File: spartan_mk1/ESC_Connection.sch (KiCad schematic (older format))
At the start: 2 parts

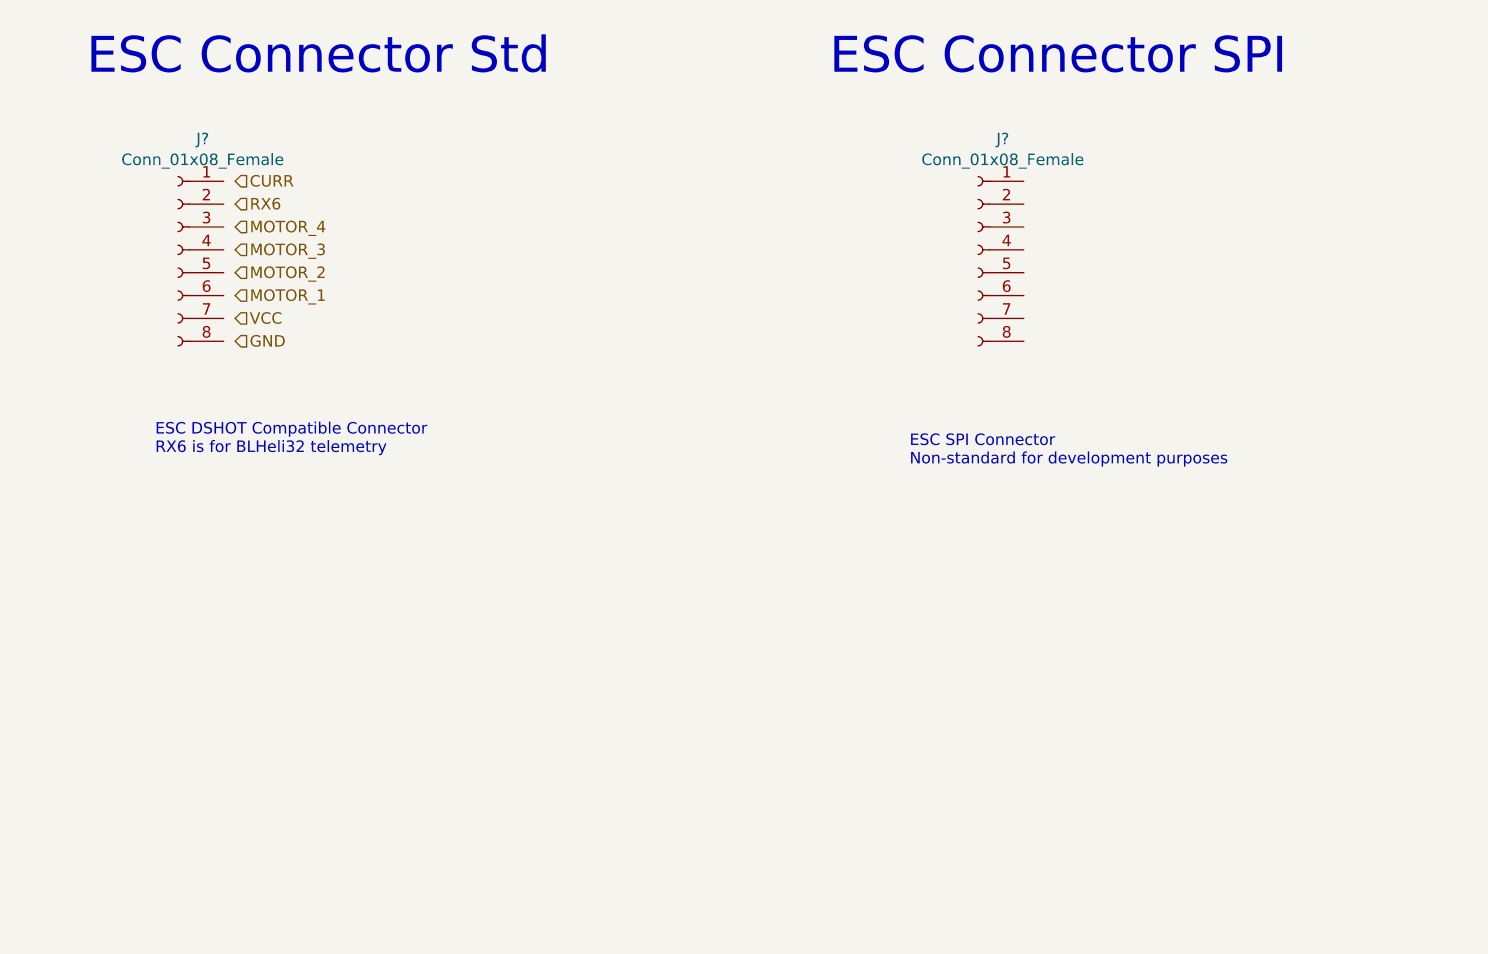
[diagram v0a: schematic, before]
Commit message: Added ESC connectors in schematic
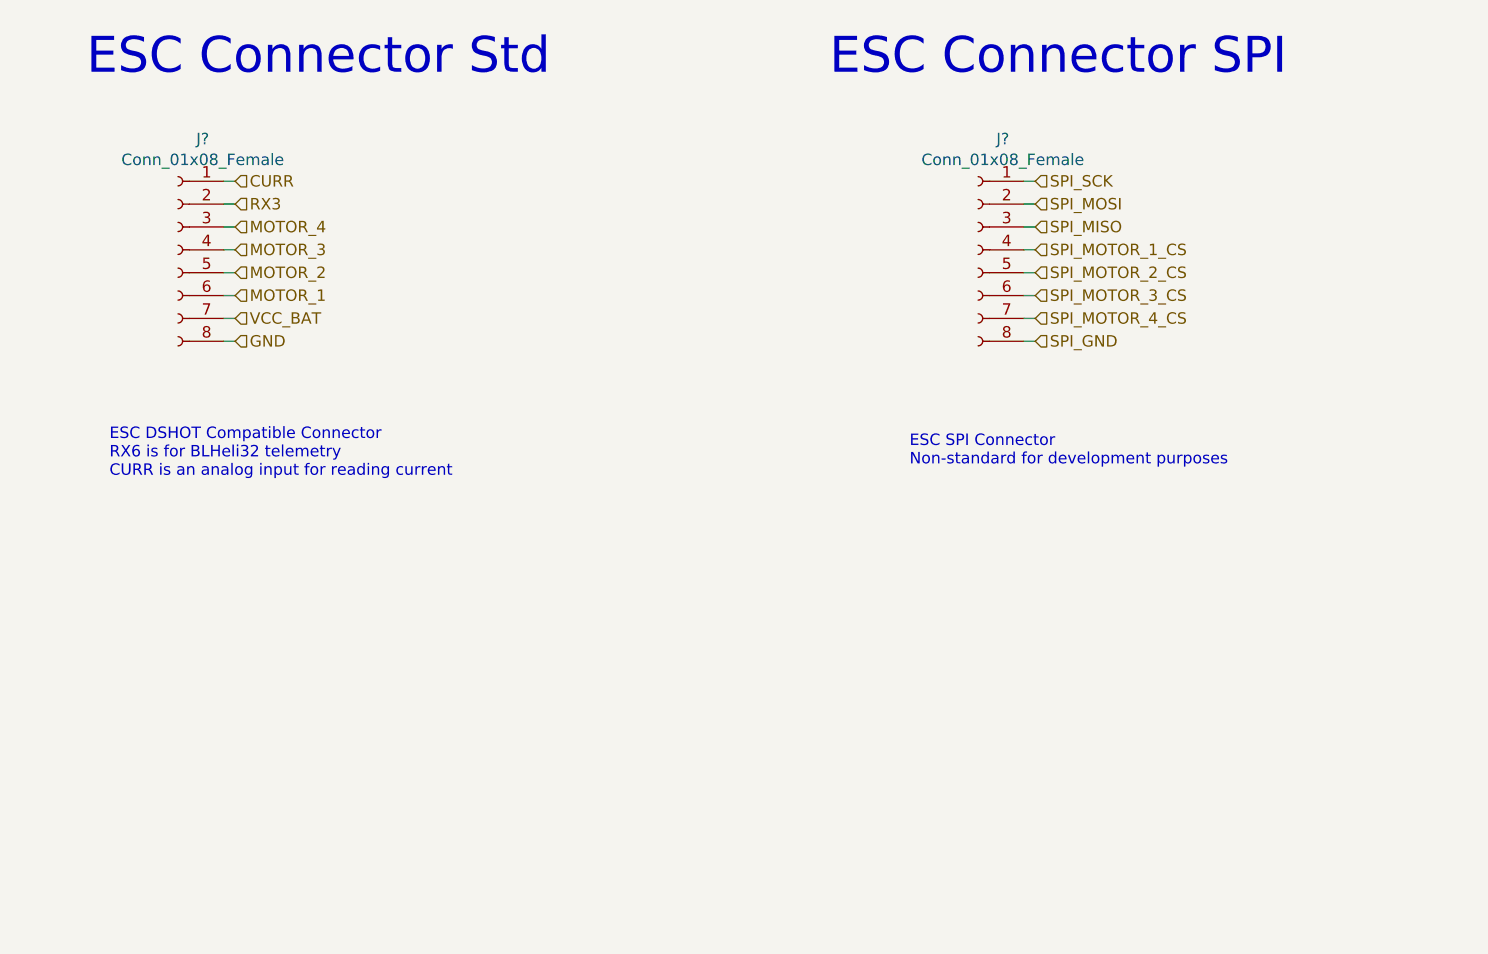
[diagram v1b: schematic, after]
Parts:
- removed J?: Conn_01x08_Female, symbol Connector:Conn_01x08_Female
- added J?: Conn_01x08_Female, symbol Connector:Conn_01x08_Female
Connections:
- net CURR: now also J?.1 (Pin_1)
- net GND: now also J?.8 (Pin_8)
- net MOTOR_1: now also J?.6 (Pin_6)
- net MOTOR_2: now also J?.5 (Pin_5)
- net MOTOR_3: now also J?.4 (Pin_4)
- net MOTOR_4: now also J?.3 (Pin_3)
- net RX3: now reaches J?.2 (Pin_2)
- net VCC_BAT: now reaches J?.7 (Pin_7)
- new net SPI_GND: J?.8 (Pin_8)
- new net SPI_MISO: J?.3 (Pin_3)
- new net SPI_MOSI: J?.2 (Pin_2)
- new net SPI_MOTOR_1_CS: J?.4 (Pin_4)
- new net SPI_MOTOR_2_CS: J?.5 (Pin_5)
- new net SPI_MOTOR_3_CS: J?.6 (Pin_6)
- new net SPI_MOTOR_4_CS: J?.7 (Pin_7)
- new net SPI_SCK: J?.1 (Pin_1)
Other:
- note added: "ESC DSHOT Compatible Connector\nRX6 is for BLHeli32 telemetry\nCURR is an analog input for reading current"
- note removed: "ESC DSHOT Compatible Connector\nRX6 is for BLHeli32 telemetry\n"
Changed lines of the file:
@@
 	-1   0    0    -1
 $EndComp
-Text Notes 3550 4000 0    50   ~ 0
-ESC DSHOT Compatible Connector\nRX6 is for BLHeli32 telemetry\n
+Text Notes 3350 4100 0    50   ~ 0
+ESC DSHOT Compatible Connector\nRX6 is for BLHeli32 telemetry\nCURR is an analog input for reading current
 Text Notes 3250 2350 0    157  ~ 0
 ESC Connector Std
 Text Notes 6500 2350 0    157  ~ 0
 ESC Connector SPI
-$Comp
-L Connector:Conn_01x08_Female J?
-U 1 1 5FC07A5E
-P 7150 3100
-F 0 "J?" H 7042 3585 50  0000 C CNN
-F 1 "Conn_01x08_Female" H 7042 3494 50  0000 C CNN
-F 2 "" H 7150 3100 50  0001 C CNN
-F 3 "~" H 7150 3100 50  0001 C CNN
-	1    7150 3100
-	-1   0    0    -1
-$EndComp
 Text Notes 6850 4050 0    50   ~ 0
 ESC SPI Connector\nNon-standard for development purposes\n
@@
 GND
 Text HLabel 3900 3400 2    50   Input ~ 0
-VCC
+VCC_BAT
 Text HLabel 3900 3300 2    50   Input ~ 0
 MOTOR_1
@@
 MOTOR_4
 Text HLabel 3900 2900 2    50   Input ~ 0
-RX6
+RX3
 Text HLabel 3900 2800 2    50   Input ~ 0
 CURR
+Wire Wire Line
+	3900 3500 3850 3500
+Wire Wire Line
+	3900 3400 3850 3400
+Wire Wire Line
+	3900 3300 3850 3300
+Wire Wire Line
+	3900 3200 3850 3200
+Wire Wire Line
+	3900 3100 3850 3100
+Wire Wire Line
+	3900 3000 3850 3000
+Wire Wire Line
+	3900 2900 3850 2900
+Wire Wire Line
+	3900 2800 3850 2800
+Wire Wire Line
+	7400 2800 7350 2800
+Text HLabel 7400 2800 2    50   Input ~ 0
+SPI_SCK
+Text HLabel 7400 2900 2    50   Input ~ 0
+SPI_MOSI
+Text HLabel 7400 3000 2    50   Input ~ 0
+SPI_MISO
+Wire Wire Line
+	7400 2900 7350 2900
+Wire Wire Line
+	7400 3000 7350 3000
+Text HLabel 7400 3100 2    50   Input ~ 0
+SPI_MOTOR_1_CS
+Text HLabel 7400 3200 2    50   Input ~ 0
+SPI_MOTOR_2_CS
+Text HLabel 7400 3300 2    50   Input ~ 0
+SPI_MOTOR_3_CS
+Text HLabel 7400 3400 2    50   Input ~ 0
+SPI_MOTOR_4_CS
+Wire Wire Line
+	7400 3100 7350 3100
+Wire Wire Line
+	7400 3200 7350 3200
+Wire Wire Line
+	7400 3300 7350 3300
+Wire Wire Line
+	7400 3400 7350 3400
+Text HLabel 7400 3500 2    50   Input ~ 0
+SPI_GND
+Wire Wire Line
+	7400 3500 7350 3500
+$Comp
+L Connector:Conn_01x08_Female J?
+U 1 1 5F8D6084
+P 7150 3100
+F 0 "J?" H 7042 3585 50  0000 C CNN
+F 1 "Conn_01x08_Female" H 7042 3494 50  0000 C CNN
+F 2 "" H 7150 3100 50  0001 C CNN
+F 3 "~" H 7150 3100 50  0001 C CNN
+	1    7150 3100
+	-1   0    0    -1
+$EndComp
 $EndSCHEMATC

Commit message: Complete schematic with DRC done
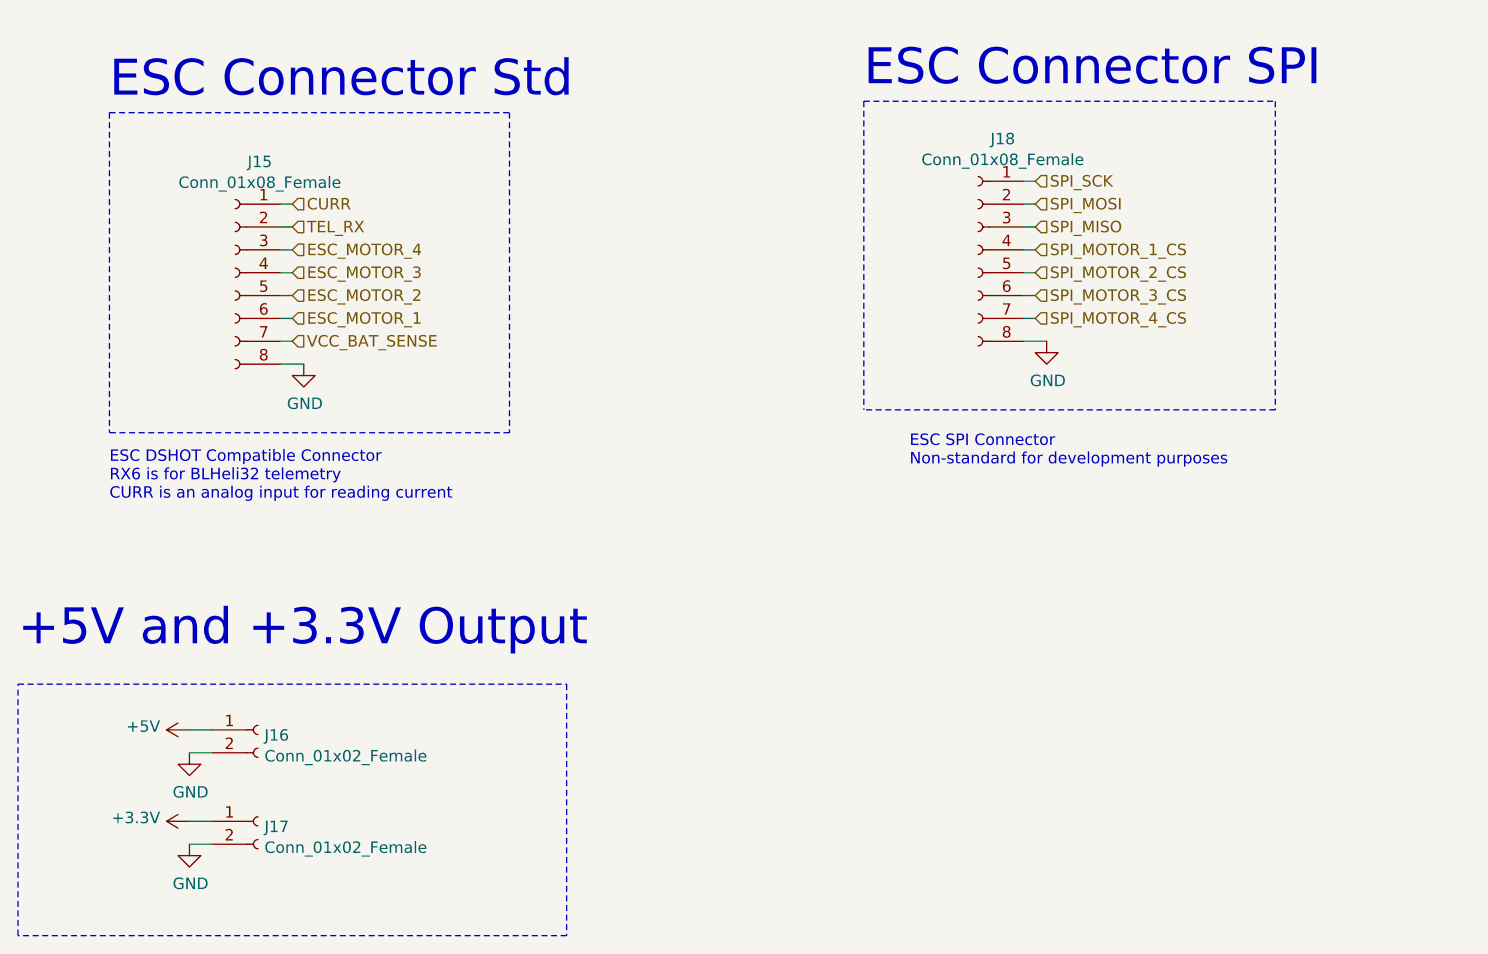
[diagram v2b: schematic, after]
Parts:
- added J16, J17: Conn_01x02_Female, symbol Connector:Conn_01x02_Female
- gave numbers to parts that had none: 2
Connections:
- net SPI_GND is gone; now on net GND: J18.8 (Pin_8)
- net GND: now also J16.2 (Pin_2), J17.2 (Pin_2)
- net MOTOR_1 renamed ESC_MOTOR_1
- net MOTOR_2 renamed ESC_MOTOR_2
- net MOTOR_3 renamed ESC_MOTOR_3
- net MOTOR_4 renamed ESC_MOTOR_4
- net RX3 renamed TEL_RX
- net VCC_BAT renamed VCC_BAT_SENSE
- new net +3V3: J17.1 (Pin_1)
- new net +5V: J16.1 (Pin_1)
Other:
- note added: "+5V and +3.3V Output"
- moved on the sheet: J15
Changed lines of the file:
@@
 $Descr A4 11693 8268
 encoding utf-8
-Sheet 5 6
+Sheet 6 6
 Title ""
 Date ""
@@
 $EndDescr
 $Comp
-L Connector:Conn_01x08_Female J?
+L Connector:Conn_01x08_Female J15
 U 1 1 5FC05E26
-P 3650 3100
-F 0 "J?" H 3542 3585 50  0000 C CNN
-F 1 "Conn_01x08_Female" H 3542 3494 50  0000 C CNN
-F 2 "" H 3650 3100 50  0001 C CNN
-F 3 "~" H 3650 3100 50  0001 C CNN
-	1    3650 3100
+P 3900 3200
+F 0 "J15" H 3792 3685 50  0000 C CNN
+F 1 "Conn_01x08_Female" H 3792 3594 50  0000 C CNN
+F 2 "" H 3900 3200 50  0001 C CNN
+F 3 "~" H 3900 3200 50  0001 C CNN
+	1    3900 3200
 	-1   0    0    -1
 $EndComp
-Text Notes 3350 4100 0    50   ~ 0
+Text Notes 3350 4200 0    50   ~ 0
 ESC DSHOT Compatible Connector\nRX6 is for BLHeli32 telemetry\nCURR is an analog input for reading current
-Text Notes 3250 2350 0    157  ~ 0
+Text Notes 3350 2450 0    157  ~ 0
 ESC Connector Std
-Text Notes 6500 2350 0    157  ~ 0
+Text Notes 6650 2400 0    157  ~ 0
 ESC Connector SPI
 Text Notes 6850 4050 0    50   ~ 0
 ESC SPI Connector\nNon-standard for development purposes\n
-Text HLabel 3900 3500 2    50   Input ~ 0
-GND
-Text HLabel 3900 3400 2    50   Input ~ 0
-VCC_BAT
-Text HLabel 3900 3300 2    50   Input ~ 0
-MOTOR_1
-Text HLabel 3900 3200 2    50   Input ~ 0
-MOTOR_2
-Text HLabel 3900 3100 2    50   Input ~ 0
-MOTOR_3
-Text HLabel 3900 3000 2    50   Input ~ 0
-MOTOR_4
-Text HLabel 3900 2900 2    50   Input ~ 0
-RX3
-Text HLabel 3900 2800 2    50   Input ~ 0
+Text HLabel 4150 3500 2    50   Input ~ 0
+VCC_BAT_SENSE
+Text HLabel 4150 3400 2    50   Input ~ 0
+ESC_MOTOR_1
+Text HLabel 4150 3300 2    50   Input ~ 0
+ESC_MOTOR_2
+Text HLabel 4150 3200 2    50   Input ~ 0
+ESC_MOTOR_3
+Text HLabel 4150 3100 2    50   Input ~ 0
+ESC_MOTOR_4
+Text HLabel 4150 3000 2    50   Input ~ 0
+TEL_RX
+Text HLabel 4150 2900 2    50   Input ~ 0
 CURR
 Wire Wire Line
-	3900 3500 3850 3500
-Wire Wire Line
-	3900 3400 3850 3400
-Wire Wire Line
-	3900 3300 3850 3300
-Wire Wire Line
-	3900 3200 3850 3200
-Wire Wire Line
-	3900 3100 3850 3100
-Wire Wire Line
-	3900 3000 3850 3000
-Wire Wire Line
-	3900 2900 3850 2900
-Wire Wire Line
-	3900 2800 3850 2800
+	4150 3400 4100 3400
+Wire Wire Line
+	4150 3300 4100 3300
+Wire Wire Line
+	4150 3200 4100 3200
+Wire Wire Line
+	4150 3100 4100 3100
 Wire Wire Line
 	7400 2800 7350 2800
@@
 Wire Wire Line
 	7400 3400 7350 3400
-Text HLabel 7400 3500 2    50   Input ~ 0
-SPI_GND
-Wire Wire Line
-	7400 3500 7350 3500
-$Comp
-L Connector:Conn_01x08_Female J?
+$Comp
+L Connector:Conn_01x08_Female J18
 U 1 1 5F8D6084
 P 7150 3100
-F 0 "J?" H 7042 3585 50  0000 C CNN
+F 0 "J18" H 7042 3585 50  0000 C CNN
 F 1 "Conn_01x08_Female" H 7042 3494 50  0000 C CNN
 F 2 "" H 7150 3100 50  0001 C CNN
@@
 	-1   0    0    -1
 $EndComp
+$Comp
+L Connector:Conn_01x02_Female J?
+U 1 1 5F94A9E6
+P 4000 5200
+AR Path="/5F78701C/5F94A9E6" Ref="J?"  Part="1"
+AR Path="/5F79A745/5F94A9E6" Ref="J?"  Part="1"
+AR Path="/5FB6E842/5F94A9E6" Ref="J16"  Part="1"
+F 0 "J16" H 4028 5176 50  0000 L CNN
+F 1 "Conn_01x02_Female" H 4028 5085 50  0000 L CNN
+F 2 "" H 4000 5200 50  0001 C CNN
+F 3 "~" H 4000 5200 50  0001 C CNN
+	1    4000 5200
+	1    0    0    -1
+$EndComp
+$Comp
+L Connector:Conn_01x02_Female J?
+U 1 1 5F94A9EC
+P 4000 5600
+AR Path="/5F78701C/5F94A9EC" Ref="J?"  Part="1"
+AR Path="/5F79A745/5F94A9EC" Ref="J?"  Part="1"
+AR Path="/5FB6E842/5F94A9EC" Ref="J17"  Part="1"
+F 0 "J17" H 4028 5576 50  0000 L CNN
+F 1 "Conn_01x02_Female" H 4028 5485 50  0000 L CNN
+F 2 "" H 4000 5600 50  0001 C CNN
+F 3 "~" H 4000 5600 50  0001 C CNN
+	1    4000 5600
+	1    0    0    -1
+$EndComp
+Wire Wire Line
+	3700 5200 3800 5200
+Wire Wire Line
+	3800 5600 3700 5600
+$Comp
+L power:GND #PWR?
+U 1 1 5F94A9F4
+P 3700 5300
+AR Path="/5F78701C/5F94A9F4" Ref="#PWR?"  Part="1"
+AR Path="/5F79A745/5F94A9F4" Ref="#PWR?"  Part="1"
+AR Path="/5FB6E842/5F94A9F4" Ref="#PWR067"  Part="1"
+F 0 "#PWR067" H 3700 5050 50  0001 C CNN
+F 1 "GND" H 3705 5127 50  0000 C CNN
+F 2 "" H 3700 5300 50  0001 C CNN
+F 3 "" H 3700 5300 50  0001 C CNN
+	1    3700 5300
+	1    0    0    -1
+$EndComp
+$Comp
+L power:GND #PWR?
+U 1 1 5F94A9FA
+P 3700 5700
+AR Path="/5F78701C/5F94A9FA" Ref="#PWR?"  Part="1"
+AR Path="/5F79A745/5F94A9FA" Ref="#PWR?"  Part="1"
+AR Path="/5FB6E842/5F94A9FA" Ref="#PWR069"  Part="1"
+F 0 "#PWR069" H 3700 5450 50  0001 C CNN
+F 1 "GND" H 3705 5527 50  0000 C CNN
+F 2 "" H 3700 5700 50  0001 C CNN
+F 3 "" H 3700 5700 50  0001 C CNN
+	1    3700 5700
+	1    0    0    -1
+$EndComp
+Wire Wire Line
+	3800 5700 3700 5700
+Wire Wire Line
+	3700 5300 3800 5300
+$Comp
+L power:+5V #PWR?
+U 1 1 5F94AA02
+P 3700 5200
+AR Path="/5F78701C/5F94AA02" Ref="#PWR?"  Part="1"
+AR Path="/5F79A745/5F94AA02" Ref="#PWR?"  Part="1"
+AR Path="/5FB6E842/5F94AA02" Ref="#PWR066"  Part="1"
+F 0 "#PWR066" H 3700 5050 50  0001 C CNN
+F 1 "+5V" V 3715 5328 50  0000 L CNN
+F 2 "" H 3700 5200 50  0001 C CNN
+F 3 "" H 3700 5200 50  0001 C CNN
+	1    3700 5200
+	0    -1   -1   0
+$EndComp
+$Comp
+L power:+3.3V #PWR?
+U 1 1 5F94AA08
+P 3700 5600
+AR Path="/5F78701C/5F94AA08" Ref="#PWR?"  Part="1"
+AR Path="/5F79A745/5F94AA08" Ref="#PWR?"  Part="1"
+AR Path="/5FB6E842/5F94AA08" Ref="#PWR068"  Part="1"
+F 0 "#PWR068" H 3700 5450 50  0001 C CNN
+F 1 "+3.3V" V 3715 5728 50  0000 L CNN
+F 2 "" H 3700 5600 50  0001 C CNN
+F 3 "" H 3700 5600 50  0001 C CNN
+	1    3700 5600
+	0    -1   -1   0
+$EndComp
+Wire Notes Line
+	3350 2500 5100 2500
+Wire Notes Line
+	6650 2450 8450 2450
+Text Notes 2950 4850 0    157  ~ 0
++5V and +3.3V Output
+Wire Notes Line
+	2950 5000 5350 5000
+Wire Notes Line
+	5350 5000 5350 6100
+Wire Notes Line
+	5350 6100 2950 6100
+Wire Notes Line
+	2950 6100 2950 5000
+$Comp
+L power:GND #PWR?
+U 1 1 5F94C089
+P 7450 3500
+AR Path="/5F78701C/5F94C089" Ref="#PWR?"  Part="1"
+AR Path="/5F79A745/5F94C089" Ref="#PWR?"  Part="1"
+AR Path="/5FB6E842/5F94C089" Ref="#PWR071"  Part="1"
+F 0 "#PWR071" H 7450 3250 50  0001 C CNN
+F 1 "GND" H 7455 3327 50  0000 C CNN
+F 2 "" H 7450 3500 50  0001 C CNN
+F 3 "" H 7450 3500 50  0001 C CNN
+	1    7450 3500
+	1    0    0    -1
+$EndComp
+Wire Wire Line
+	7350 3500 7450 3500
+Wire Notes Line
+	8450 3800 6650 3800
+Wire Notes Line
+	6650 2450 6650 3800
+Wire Notes Line
+	8450 2450 8450 3800
+$Comp
+L power:GND #PWR?
+U 1 1 5F98AC2C
+P 4200 3600
+AR Path="/5F78701C/5F98AC2C" Ref="#PWR?"  Part="1"
+AR Path="/5F79A745/5F98AC2C" Ref="#PWR?"  Part="1"
+AR Path="/5FB6E842/5F98AC2C" Ref="#PWR070"  Part="1"
+F 0 "#PWR070" H 4200 3350 50  0001 C CNN
+F 1 "GND" H 4205 3427 50  0000 C CNN
+F 2 "" H 4200 3600 50  0001 C CNN
+F 3 "" H 4200 3600 50  0001 C CNN
+	1    4200 3600
+	1    0    0    -1
+$EndComp
+Wire Wire Line
+	4100 3600 4200 3600
+Wire Notes Line
+	5100 3900 3350 3900
+Wire Notes Line
+	3350 2500 3350 3900
+Wire Notes Line
+	5100 2500 5100 3900
+Wire Wire Line
+	4100 3500 4150 3500
+Wire Wire Line
+	4100 3000 4150 3000
+Wire Wire Line
+	4100 2900 4150 2900
 $EndSCHEMATC

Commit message: Footprints added started PCB placement
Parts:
- J15, J18: footprint (none) -> Connector_JST:JST_SH_BM08B-SRSS-TB_1x08-1MP_P1.00mm_Vertical
- J16, J17: footprint (none) -> Connector_PinHeader_2.54mm:PinHeader_1x02_P2.54mm_Vertical
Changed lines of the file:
@@
 F 0 "J15" H 3792 3685 50  0000 C CNN
 F 1 "Conn_01x08_Female" H 3792 3594 50  0000 C CNN
-F 2 "" H 3900 3200 50  0001 C CNN
+F 2 "Connector_JST:JST_SH_BM08B-SRSS-TB_1x08-1MP_P1.00mm_Vertical" H 3900 3200 50  0001 C CNN
 F 3 "~" H 3900 3200 50  0001 C CNN
 	1    3900 3200
@@
 F 0 "J18" H 7042 3585 50  0000 C CNN
 F 1 "Conn_01x08_Female" H 7042 3494 50  0000 C CNN
-F 2 "" H 7150 3100 50  0001 C CNN
+F 2 "Connector_JST:JST_SH_BM08B-SRSS-TB_1x08-1MP_P1.00mm_Vertical" H 7150 3100 50  0001 C CNN
 F 3 "~" H 7150 3100 50  0001 C CNN
 	1    7150 3100
@@
 F 0 "J16" H 4028 5176 50  0000 L CNN
 F 1 "Conn_01x02_Female" H 4028 5085 50  0000 L CNN
-F 2 "" H 4000 5200 50  0001 C CNN
+F 2 "Connector_PinHeader_2.54mm:PinHeader_1x02_P2.54mm_Vertical" H 4000 5200 50  0001 C CNN
 F 3 "~" H 4000 5200 50  0001 C CNN
 	1    4000 5200
@@
 F 0 "J17" H 4028 5576 50  0000 L CNN
 F 1 "Conn_01x02_Female" H 4028 5485 50  0000 L CNN
-F 2 "" H 4000 5600 50  0001 C CNN
+F 2 "Connector_PinHeader_2.54mm:PinHeader_1x02_P2.54mm_Vertical" H 4000 5600 50  0001 C CNN
 F 3 "~" H 4000 5600 50  0001 C CNN
 	1    4000 5600
